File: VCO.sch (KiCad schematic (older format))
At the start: 55 parts, among them J1 Conn_01x05_Male, J10 FM, J11 Conn_01x05_Male, J12 PW, J13 saw, J14 sq, J2 Conn_01x05_Male, J3 V/oct, J4 Conn_01x05_Male, J5 Conn_01x05_Male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

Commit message: 3d model ready
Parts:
- RV4: footprint footprint:PTV09A4020FB103 -> footprint:R0904N
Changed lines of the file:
@@
 F 0 "RV4" H 2280 891 50  0000 R CNN
 F 1 "10K" H 2280 800 50  0000 R CNN
-F 2 "footprint:PTV09A4020FB103" H 2350 800 50  0001 C CNN
+F 2 "footprint:R0904N" H 2350 800 50  0001 C CNN
 F 3 "~" H 2350 800 50  0001 C CNN
 F 4 "R0904N-A10K" H 2250 650 50  0000 R CNN "Тип"

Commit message: refactor schematic
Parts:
- added R? (x7): 1K, footprint:r0603, symbol uRack:R
- added R? (x5): 100K, footprint:r0603, symbol uRack:R
- added R? (x4): 100R, footprint:r0603, symbol uRack:R
- R17: value 1K -> 100R
- R2: value 24K -> 10K
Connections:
- net labels added: cv, saw
- net labels removed: GND, OUT_1, OUT_2, PW
- wire segments 273 -> 269
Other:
- moved on the sheet: C1, C2, C4, C5, C6, J10, J12, J13, J14, Q3, R10, R11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

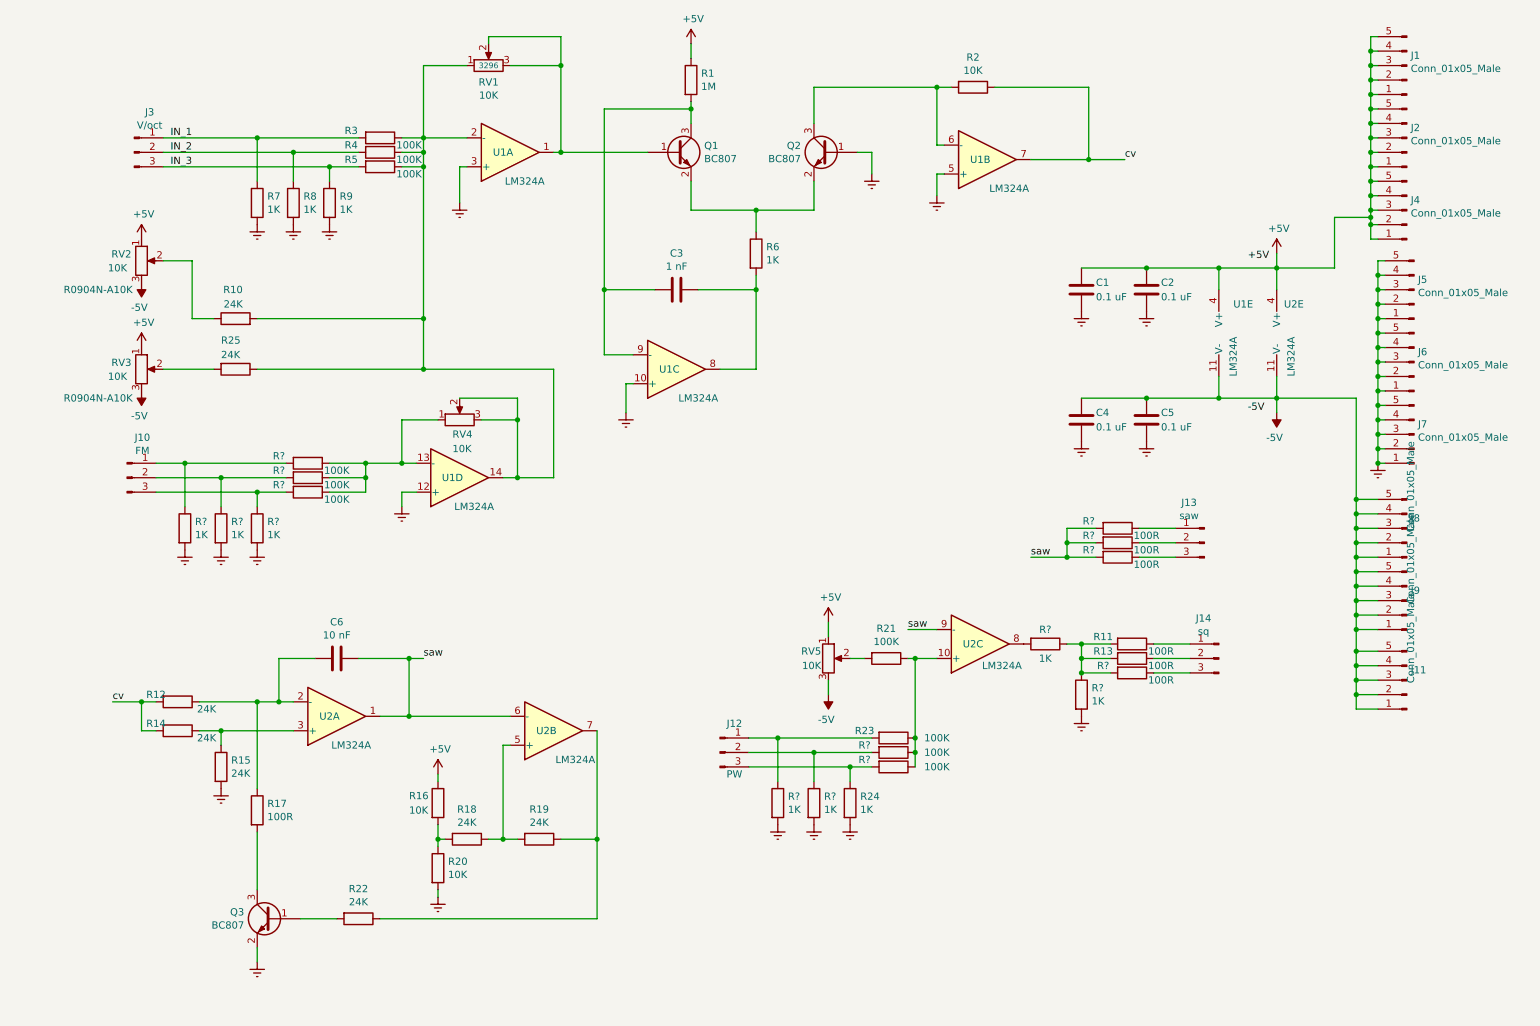
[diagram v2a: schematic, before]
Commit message: pwm and freq cv inputs
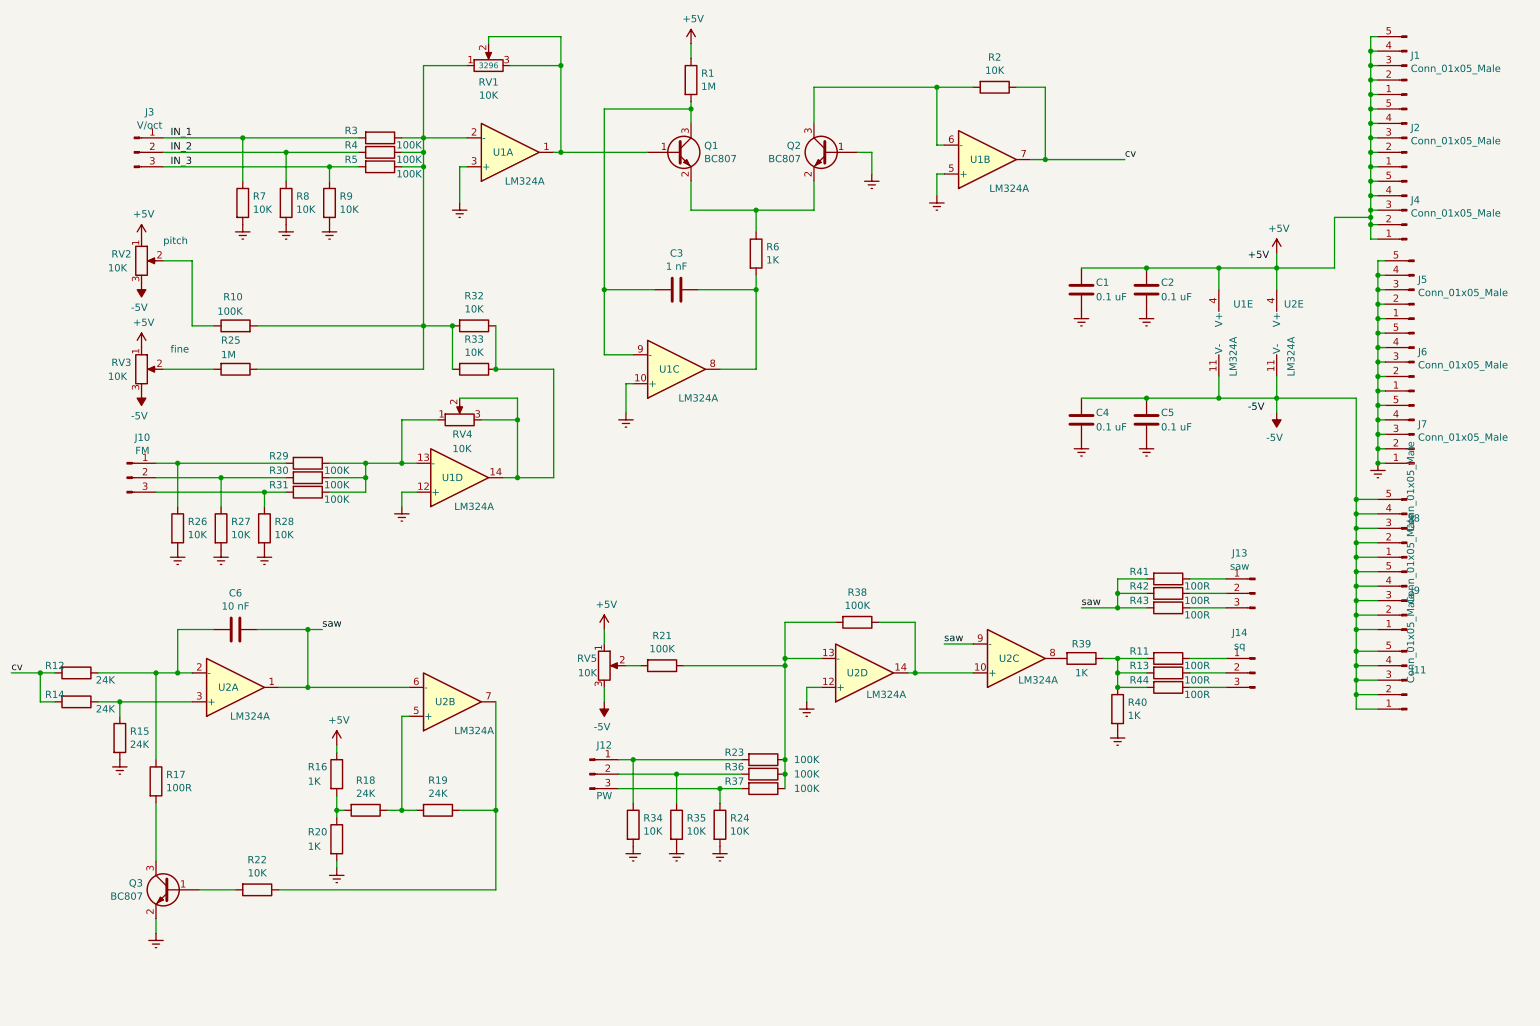
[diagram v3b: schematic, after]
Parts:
- added R32, R33: 10K, footprint:r0603, symbol uRack:R
- added R38: 100K, footprint:r0603, symbol uRack:R
- added unit 4 of U2
- R10: value 24K -> 100K
- R16, R20: value 10K -> 1K
- R22: value 24K -> 10K
- R24, R7, R8, R9: value 1K -> 10K
- R25: value 24K -> 1M
- R26, R27, R28, R34, R35: renamed from R?; value 1K -> 10K
- gave numbers to parts that had none: 11
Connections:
- net GND: now also U2.12 (+)
- net at R10.2, R25.1, R3.1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: now also R32.2, R33.2; no longer RV4.2, RV4.3, U1.14
- net at R21.1, R23.1, R36.1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: now also R38.2, U2.13 (-); no longer U2.10 (+)
- new net: R32.1, R33.1, RV4.2, RV4.3, U1.14
- new net: R38.1, U2.10 (+), U2.14
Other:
- note added: "fine"
- note added: "pitch"
- moved on the sheet: C6, J12, J13, J14, Q3, R10, R11, R12, R13, R14, R15, R16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

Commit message: change label
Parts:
- R10: value 100K -> 1M
- R16: value 1K -> 10K
- R17: value 100R -> 1K
- R18: value 24K -> 10K
- R20: value 1K -> 24K
- R25: value 1M -> 100K
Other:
- note added: "TBD: 100 ohm"
- moved on the sheet: R21, RV5
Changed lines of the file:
@@
 P 2150 2700
 F 0 "R10" V 2350 2650 50  0000 L CNN
-F 1 "100K" V 2250 2650 50  0000 L CNN
+F 1 "1M" V 2250 2650 50  0000 L CNN
 F 2 "footprint:r0603" V 2080 2700 50  0001 C CNN
 F 3 "~" H 2150 2700 50  0001 C CNN
@@
 P 1600 5850
 F 0 "R17" H 1670 5896 50  0000 L CNN
-F 1 "100R" H 1670 5805 50  0000 L CNN
+F 1 "1K" H 1670 5805 50  0000 L CNN
 F 2 "footprint:r0603" V 1530 5850 50  0001 C CNN
 F 3 "~" H 1600 5850 50  0001 C CNN
@@
 P 3050 6050
 F 0 "R18" V 2843 6050 50  0000 C CNN
-F 1 "24K" V 2934 6050 50  0000 C CNN
+F 1 "10K" V 2934 6050 50  0000 C CNN
 F 2 "footprint:r0603" V 2980 6050 50  0001 C CNN
 F 3 "~" H 3050 6050 50  0001 C CNN
@@
 P 2850 5800
 F 0 "R16" H 2650 5850 50  0000 L CNN
-F 1 "1K" H 2650 5750 50  0000 L CNN
+F 1 "10K" H 2650 5750 50  0000 L CNN
 F 2 "footprint:r0603" V 2780 5800 50  0001 C CNN
 F 3 "~" H 2850 5800 50  0001 C CNN
@@
 P 2850 6250
 F 0 "R20" H 2650 6300 50  0000 L CNN
-F 1 "1K" H 2650 6200 50  0000 L CNN
+F 1 "24K" H 2650 6200 50  0000 L CNN
 F 2 "footprint:r0603" V 2780 6250 50  0001 C CNN
 F 3 "~" H 2850 6250 50  0001 C CNN
@@
 L uRack:R_POT RV5
 U 1 1 5C748A0D
-P 4700 5050
-F 0 "RV5" H 4650 5100 50  0000 R CNN
-F 1 "10K" H 4650 5000 50  0000 R CNN
-F 2 "footprint:PTV09A4020FB103" H 4700 5050 50  0001 C CNN
-F 3 "~" H 4700 5050 50  0001 C CNN
-F 4 "R0904N-A10K" V 4450 4850 50  0001 C CNN "Тип"
-	1    4700 5050
+P 4700 5000
+F 0 "RV5" H 4650 5050 50  0000 R CNN
+F 1 "10K" H 4650 4950 50  0000 R CNN
+F 2 "footprint:PTV09A4020FB103" H 4700 5000 50  0001 C CNN
+F 3 "~" H 4700 5000 50  0001 C CNN
+F 4 "R0904N-A10K" V 4450 4800 50  0001 C CNN "Тип"
+	1    4700 5000
 	1    0    0    -1
 $EndComp
@@
 L uRack:R R21
 U 1 1 5C748C0D
-P 5100 5050
-F 0 "R21" V 4893 5050 50  0000 C CNN
-F 1 "100K" V 4984 5050 50  0000 C CNN
-F 2 "footprint:r0603" V 5030 5050 50  0001 C CNN
-F 3 "~" H 5100 5050 50  0001 C CNN
-	1    5100 5050
-	0    1    1    0
-$EndComp
-Wire Wire Line
-	4850 5050 4950 5050
+P 5100 5000
+F 0 "R21" V 4893 5000 50  0000 C CNN
+F 1 "100K" V 4984 5000 50  0000 C CNN
+F 2 "footprint:r0603" V 5030 5000 50  0001 C CNN
+F 3 "~" H 5100 5000 50  0001 C CNN
+	1    5100 5000
+	0    1    1    0
+$EndComp
+Wire Wire Line
+	4850 5000 4950 5000
 $Comp
 L uRack:GNDREF #PWR021
@@
 L uRack:-5V #PWR019
 U 1 1 5C7578A1
-P 4700 5300
-F 0 "#PWR019" H 4700 5400 50  0001 C CNN
-F 1 "-5V" H 4715 5473 50  0000 C CNN
-F 2 "" H 4700 5300 50  0001 C CNN
-F 3 "" H 4700 5300 50  0001 C CNN
-	1    4700 5300
+P 4700 5250
+F 0 "#PWR019" H 4700 5350 50  0001 C CNN
+F 1 "-5V" H 4715 5423 50  0000 C CNN
+F 2 "" H 4700 5250 50  0001 C CNN
+F 3 "" H 4700 5250 50  0001 C CNN
+	1    4700 5250
 	-1   0    0    1
 $EndComp
@@
 L uRack:+5V #PWR017
 U 1 1 5C757966
-P 4700 4800
-F 0 "#PWR017" H 4700 4650 50  0001 C CNN
-F 1 "+5V" H 4715 4973 50  0000 C CNN
-F 2 "" H 4700 4800 50  0001 C CNN
-F 3 "" H 4700 4800 50  0001 C CNN
-	1    4700 4800
-	1    0    0    -1
-$EndComp
-Wire Wire Line
-	4700 4800 4700 4900
-Wire Wire Line
-	4700 5200 4700 5300
+P 4700 4750
+F 0 "#PWR017" H 4700 4600 50  0001 C CNN
+F 1 "+5V" H 4715 4923 50  0000 C CNN
+F 2 "" H 4700 4750 50  0001 C CNN
+F 3 "" H 4700 4750 50  0001 C CNN
+	1    4700 4750
+	1    0    0    -1
+$EndComp
+Wire Wire Line
+	4700 4750 4700 4850
+Wire Wire Line
+	4700 5150 4700 5250
 $Comp
 L uRack:R_POT RV4
@@
 P 2150 3000
 F 0 "R25" V 1950 2900 50  0000 L CNN
-F 1 "1M" V 2050 2900 50  0000 L CNN
+F 1 "100K" V 2050 2900 50  0000 L CNN
 F 2 "footprint:r0603" V 2080 3000 50  0001 C CNN
 F 3 "~" H 2150 3000 50  0001 C CNN
@@
 	1    0    0    -1
 $EndComp
-Text Notes 1650 2150 0    50   ~ 0
+Text Notes 1650 2900 0    50   ~ 0
 pitch
-Text Notes 1700 2900 0    50   ~ 0
+Text Notes 1700 2150 0    50   ~ 0
 fine
 $Comp
@@
 Wire Wire Line
 	6100 5200 6100 5300
-Wire Wire Line
-	5950 5050 5950 5700
 Connection ~ 5950 5700
 Wire Wire Line
-	5250 5050 5950 5050
+	5250 5000 5950 5000
 Wire Wire Line
 	6200 5200 6100 5200
 Wire Wire Line
 	6200 5000 5950 5000
-Wire Wire Line
-	5950 5000 5950 5050
-Connection ~ 5950 5050
 Wire Wire Line
 	6800 5100 6850 5100
@@
 	5950 4750 5950 5000
 Connection ~ 5950 5000
+Text Notes 1650 6050 0    50   ~ 0
+TBD: 100 ohm
+Wire Wire Line
+	5950 5000 5950 5700
 $EndSCHEMATC
